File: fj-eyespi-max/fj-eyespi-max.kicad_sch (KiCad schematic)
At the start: 2 parts, among them J1 Conn_01x18_Socket, J2 Conn_02x16_Odd_Even

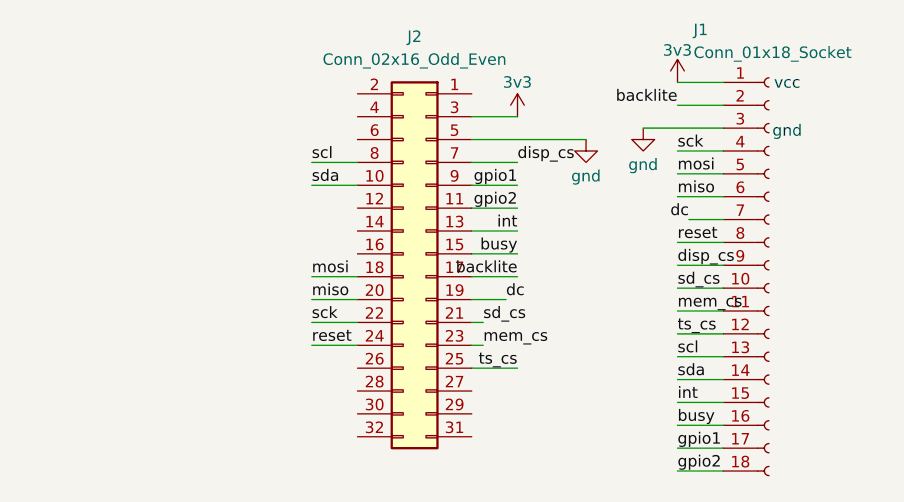
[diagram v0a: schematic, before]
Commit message: total remix
min and max boards re-routed and date, new silks....
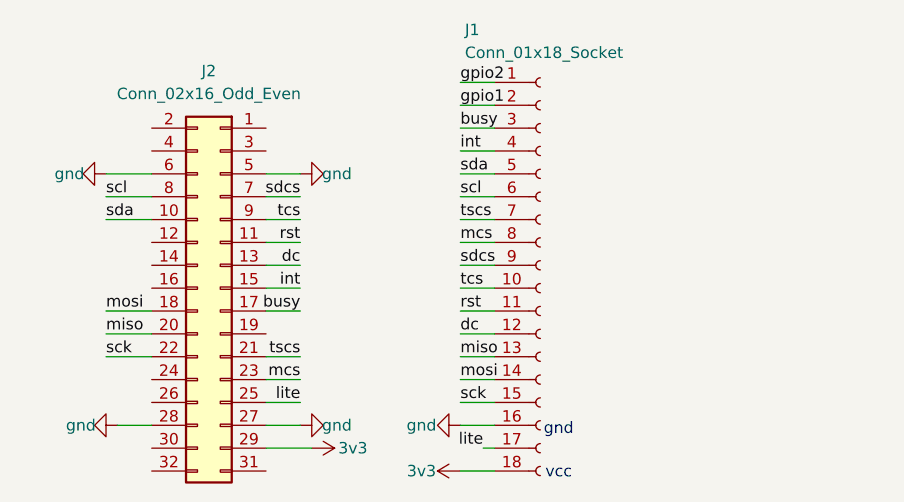
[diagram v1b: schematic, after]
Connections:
- net 3v3: now also J1.18 (Pin_18), J2.29 (Pin_29); no longer J1.1 (Pin_1), J2.3 (Pin_3)
- net busy: now also J1.3 (Pin_3), J2.17 (Pin_17); no longer J1.16 (Pin_16), J2.15 (Pin_15)
- net dc: now also J1.12 (Pin_12), J2.13 (Pin_13); no longer J1.7 (Pin_7), J2.19 (Pin_19)
- net gnd: now also J1.16 (Pin_16), J2.27 (Pin_27), J2.28 (Pin_28), J2.6 (Pin_6); no longer J1.3 (Pin_3)
- net gpio1: now also J1.2 (Pin_2); no longer J1.17 (Pin_17), J2.9 (Pin_9)
- net gpio2: now also J1.1 (Pin_1); no longer J1.18 (Pin_18), J2.11 (Pin_11)
- net int: now also J1.4 (Pin_4), J2.15 (Pin_15); no longer J1.15 (Pin_15), J2.13 (Pin_13)
- net miso: now also J1.13 (Pin_13); no longer J1.6 (Pin_6)
- net mosi: now also J1.14 (Pin_14); no longer J1.5 (Pin_5)
- net sck: now also J1.15 (Pin_15); no longer J1.4 (Pin_4)
- net scl: now also J1.6 (Pin_6); no longer J1.13 (Pin_13)
- net sda: now also J1.5 (Pin_5); no longer J1.14 (Pin_14)
- removed net backlite: J1.2 (Pin_2), J2.17 (Pin_17)
- net disp_cs renamed sdcs
- net mem_cs renamed mcs
- net mcs: now also J1.8 (Pin_8); no longer J1.11 (Pin_11)
- net reset: no longer names the net of J2.24 (Pin_24)
- net reset: no longer J1.8 (Pin_8)
- net sd_cs renamed tcs
- net tcs: now also J2.9 (Pin_9); no longer J2.21 (Pin_21)
- net ts_cs renamed lite
- net lite: now also J1.17 (Pin_17); no longer J1.12 (Pin_12)
- new net rst: J1.11 (Pin_11), J2.11 (Pin_11)
- new net tscs: J1.7 (Pin_7), J2.21 (Pin_21)

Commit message: re-routing
still had some flipped pins switching to max only
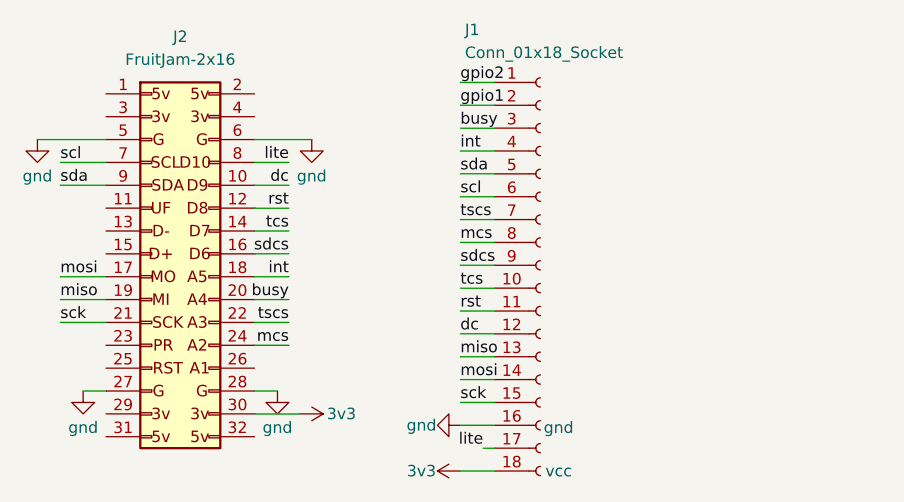
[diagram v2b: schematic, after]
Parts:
- removed J2: Conn_02x16_Odd_Even, Connector_PinHeader_2.54mm:PinHeader_2x16_P2.54mm_Vertical_SMD, symbol Connector_Generic:Conn_02x16_Odd_Even
- added J2: FruitJam-2x16, Connector_PinHeader_2.54mm:PinHeader_2x16_P2.54mm_Vertical_SMD, symbol mikeysklar:FruitJam-2x16
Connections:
- net 3v3: now also J2.30 (Pin_30)
- net busy: now also J2.20 (Pin_20)
- net dc: now also J2.10 (Pin_10)
- net gnd: now also J2.27 (Pin_27), J2.28 (Pin_28), J2.5 (Pin_5), J2.6 (Pin_6)
- net int: now also J2.18 (Pin_18)
- net lite: now also J2.8 (Pin_8)
- net mcs: now also J2.24 (Pin_24)
- net miso: now also J2.19 (Pin_19)
- net mosi: now also J2.17 (Pin_17)
- net rst: now also J2.12 (Pin_12)
- net sck: now also J2.21 (Pin_21)
- net scl: now also J2.7 (Pin_7)
- net sda: now also J2.9 (Pin_9)
- net sdcs: now also J2.16 (Pin_16)
- net tcs: now also J2.14 (Pin_14)
- net tscs: now also J2.22 (Pin_22)

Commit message: re-routed max
aligned with flipped header
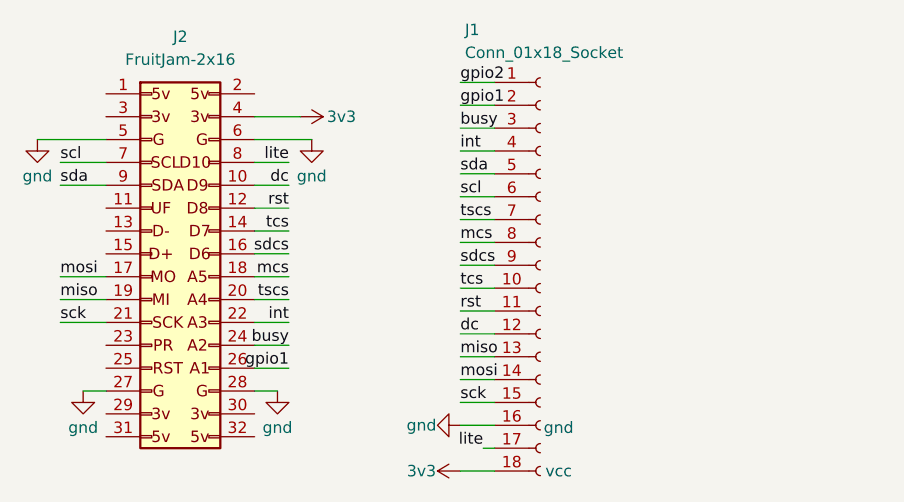
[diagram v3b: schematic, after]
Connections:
- net 3v3: now also J2.4 (Pin_4); no longer J2.30 (Pin_30)
- net busy: now also J2.24 (Pin_24); no longer J2.20 (Pin_20)
- net gpio1: now also J2.26 (Pin_26)
- net int: now also J2.22 (Pin_22); no longer J2.18 (Pin_18)
- net mcs: now also J2.18 (Pin_18); no longer J2.24 (Pin_24)
- net tscs: now also J2.20 (Pin_20); no longer J2.22 (Pin_22)
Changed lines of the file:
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@@
 	(wire
 		(pts
-			(xy 132.08 101.6) (xy 137.16 101.6)
+			(xy 135.89 96.52) (xy 132.08 96.52)
+		)
+		(stroke
+			(width 0)
+			(type default)
+		)
+	)
+	(wire
+		(pts
+			(xy 132.08 68.58) (xy 137.16 68.58)
 		)
 		(stroke
@@
 	(wire
 		(pts
-			(xy 132.08 91.44) (xy 135.89 91.44)
+			(xy 132.08 88.9) (xy 135.89 88.9)
 		)
 		(stroke
@@
 	(wire
 		(pts
-			(xy 135.89 88.9) (xy 132.08 88.9)
+			(xy 135.89 93.98) (xy 132.08 93.98)
 		)
 		(stroke
@@
 	(wire
 		(pts
-			(xy 135.89 86.36) (xy 132.08 86.36)
+			(xy 135.89 91.44) (xy 132.08 91.44)
 		)
 		(stroke
@@
 	(wire
 		(pts
-			(xy 132.08 93.98) (xy 135.89 93.98)
+			(xy 132.08 86.36) (xy 135.89 86.36)
 		)
 		(stroke
@@
 	)
 	(label "busy"
-		(at 135.89 88.9 180)
+		(at 135.89 93.98 180)
 		(effects
 			(font
@@
 	)
 	(label "mcs"
-		(at 135.89 93.98 180)
+		(at 135.89 86.36 180)
 		(effects
 			(font
@@
 		)
 	)
+	(label "gpio1"
+		(at 135.89 96.52 180)
+		(effects
+			(font
+				(size 1.27 1.27)
+			)
+			(justify right bottom)
+		)
+	)
 	(label "tscs"
-		(at 135.89 91.44 180)
+		(at 135.89 88.9 180)
 		(effects
 			(font
@@
 	)
 	(label "int"
-		(at 135.89 86.36 180)
+		(at 135.89 91.44 180)
 		(effects
 			(font
@@
 	(symbol
 		(lib_id "power:+3V3")
-		(at 137.16 101.6 270)
+		(at 137.16 68.58 270)
 		(unit 1)
 		(exclude_from_sim no)
@@
 		(dnp no)
 		(property "Reference" "#PWR017"
-			(at 133.35 101.6 0)
+			(at 133.35 68.58 0)
 			(effects
 				(font
@@
 		)
 		(property "Value" "3v3"
-			(at 141.732 101.6 90)
+			(at 141.732 68.58 90)
 			(effects
 				(font
@@
 		)
 		(property "Footprint" ""
-			(at 137.16 101.6 0)
+			(at 137.16 68.58 0)
 			(effects
 				(font
@@
 		)
 		(property "Datasheet" ""
-			(at 137.16 101.6 0)
+			(at 137.16 68.58 0)
 			(effects
 				(font
@@
 		)
 		(property "Description" "Power symbol creates a global label with name \"+3V3\""
-			(at 137.16 101.6 0)
-			(effects
-				(font
+			(at 137.16 68.58 0)
+			(effects
+				(font
